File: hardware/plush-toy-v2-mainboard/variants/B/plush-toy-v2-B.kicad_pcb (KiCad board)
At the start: 4 copper layers, 45 x 43 mm, 98 parts, among them U1 ESP32-S3-WROOM-1-N16R8

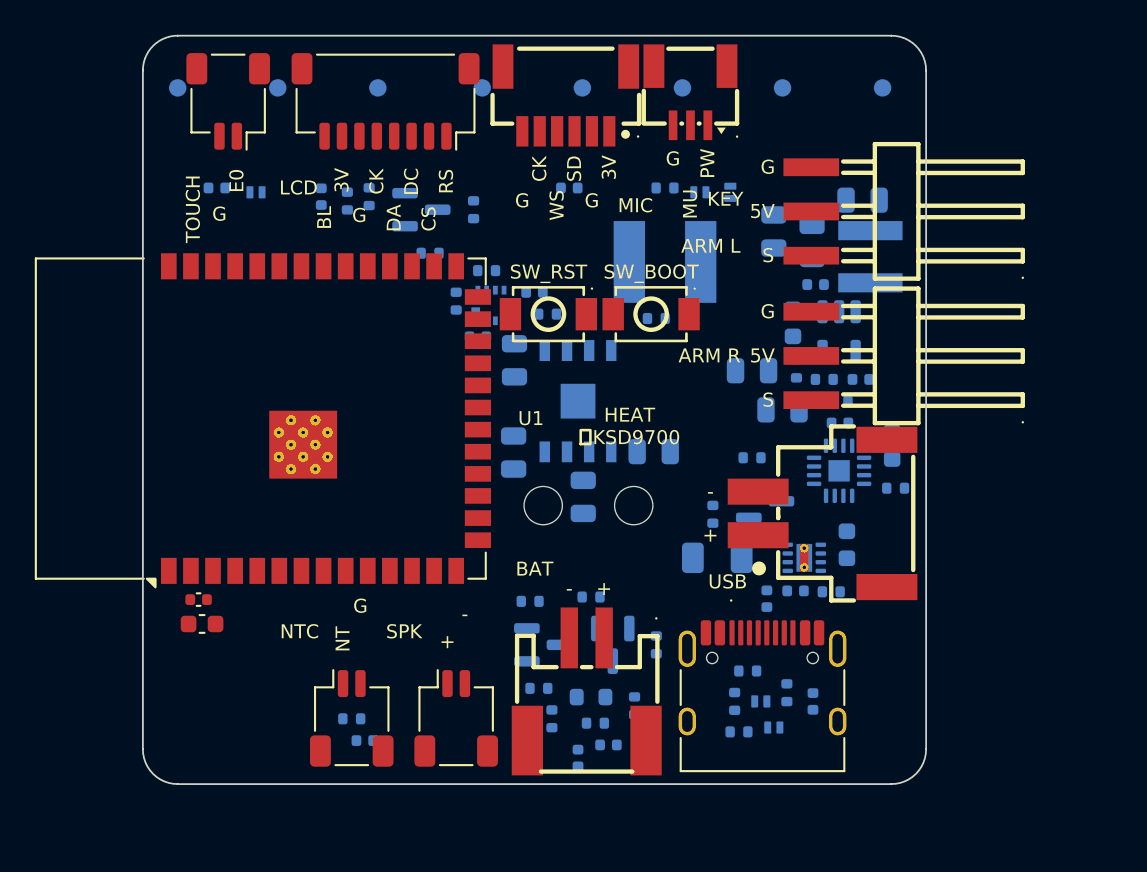
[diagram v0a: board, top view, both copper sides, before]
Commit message: feat(pcb-v2): complete order-ready variant B
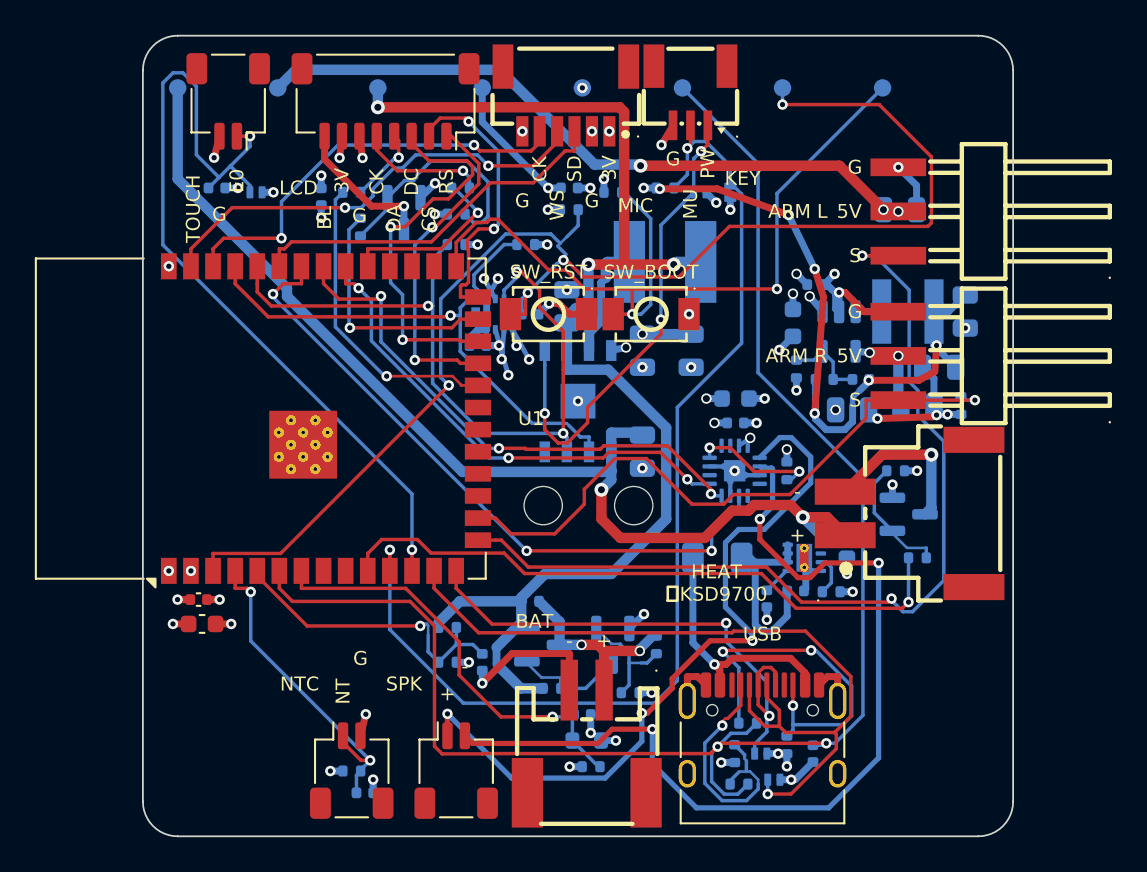
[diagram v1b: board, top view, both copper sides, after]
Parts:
- moved R_GATE 11.1 mm to (44.5, 30.0)
- moved R_GATE_PD 10.8 mm to (43.2, 25.0), turned to 0 degrees
- moved C_VSYS2 10.4 mm to (31.5, 18.1)
- moved C_BUCK_OUT2 10.3 mm to (45.8, 19.1), turned to 180 degrees
- moved R_VBAT_TOP 10.1 mm to (17.5, 34.0)
- moved C_CHG_BAT 9.73 mm to (24.4, 15.6), turned to 90 degrees
- moved C_VSYS1 9.43 mm to (28.7, 18.1)
- moved C_AMP_BULK 9.40 mm to (34.0, 20.9), turned to 0 degrees
- moved C_CHG_VIN 9.03 mm to (28.7, 23.9)
- moved C_BUCK_OUT1 8.70 mm to (47.2, 15.8), turned to -90 degrees
- moved C_VBAT_SENSE 8.67 mm to (19.5, 36.0), turned to -90 degrees
- moved Q_HEAT 8.28 mm to (44.0, 27.5)
- moved C_SERVO2 7.75 mm to (44.5, 21.2)
- moved R_BOOT 7.67 mm to (27.0, 9.00)
- moved C_SERVO1 7.36 mm to (43.5, 10.0), turned to 0 degrees
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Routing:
- net CC_SENSE: track 0.00 -> 92.2 mm, vias 0 -> 2
- net GND: track 0.00 -> 83.5 mm, vias 0 -> 57
- net EN: track 0.00 -> 79.7 mm, vias 0 -> 4
- net VBAT: track 0.00 -> 73.6 mm, vias 0 -> 3
- net VUSB: track 0.00 -> 64.1 mm, vias 0 -> 2
- net +3V3: track 0.00 -> 63.9 mm, vias 0 -> 24
- net KEY_MUTE: track 0.00 -> 63.3 mm, vias 0 -> 2
- net SPK_N: track 0.00 -> 52.9 mm, vias 0 -> 3
- net SERVO_L_PWM: track 0.00 -> 52.5 mm, vias 0 -> 2
- net VSYS: track 0.00 -> 52.0 mm, vias 0 -> 15
- net TOUCH_E0: track 0.00 -> 48.9 mm, vias 0 -> 2
- net BOOT: track 0.00 -> 47.1 mm, vias 0 -> 2
- net USB_DN: track 0.00 -> 47.1 mm, vias 0 -> 1
- net SPK_P: track 0.00 -> 42.8 mm, vias 0 -> 3
- net I2C_SDA: track 0.00 -> 42.5 mm, vias 0 -> 3
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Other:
- board size 45 x 43 mm -> 50 x 46 mm
